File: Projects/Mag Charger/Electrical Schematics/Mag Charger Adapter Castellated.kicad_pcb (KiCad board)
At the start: 2 copper layers, 26 x 12.2 mm, 4 parts, among them J1 Conn_01x08, J2 DX07S016JA3R1500

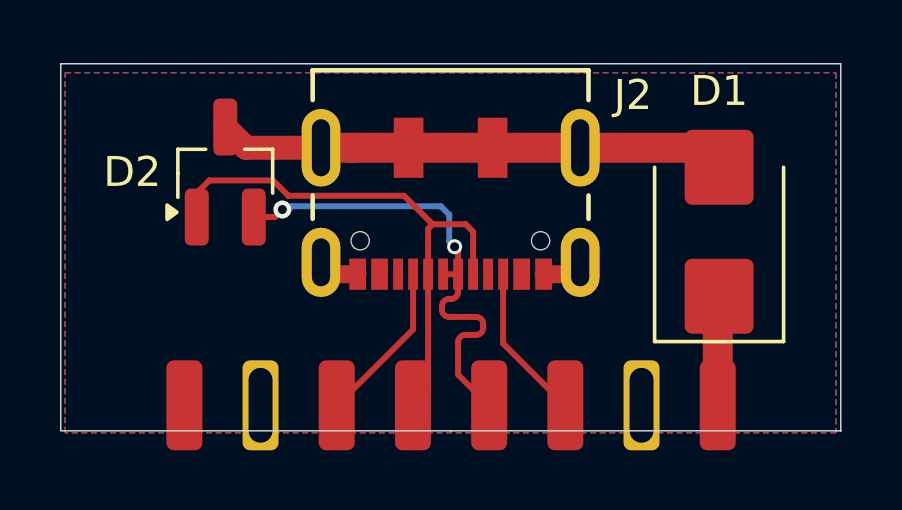
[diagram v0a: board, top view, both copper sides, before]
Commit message: Updated mag charger design
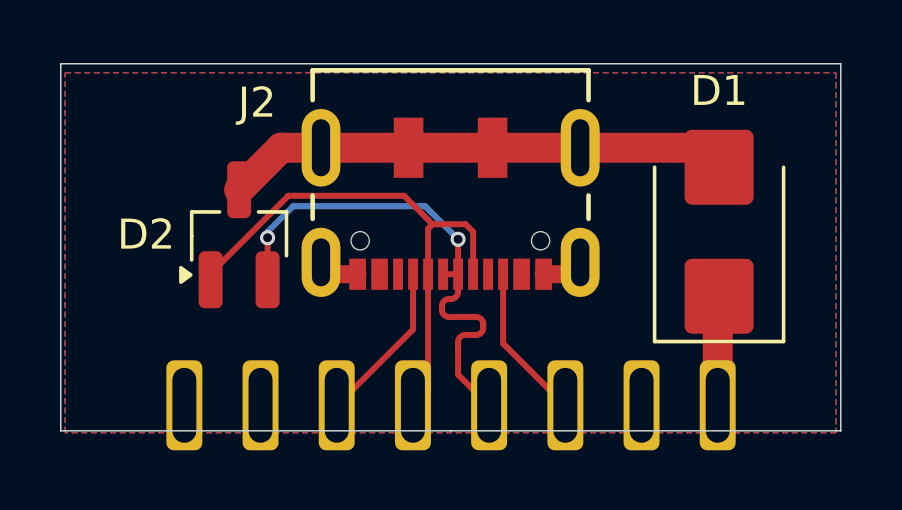
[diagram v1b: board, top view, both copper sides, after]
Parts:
- J1: moved to B.Cu
- moved D2 2.14 mm to (147.4, 139.3)
- turned J1 to 180 degrees
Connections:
- J1 pad 3: /USB_VCONN -> /USB_CC
- J1 pad 4: /USB_DN -> /USB_DP
- J1 pad 5: /USB_DP -> /USB_DN
- J1 pad 6: /USB_CC -> /USB_VCONN
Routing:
- net GND: track 20.9 -> 19.6 mm
- net /USB_DP: track 16.3 -> 17.4 mm
